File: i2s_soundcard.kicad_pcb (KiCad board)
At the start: 4 copper layers, 83.1 x 96.6 mm, 41 parts, among them J1 Conn_01x08, J2 Conn_01x06, J3 Conn_02x20_Odd_Even, J5 Conn_01x03, U1 TLV320AIC3206IRSBR, U2 TPA2006D1DRBR, U3 TPA2006D1DRBR, U4 FSA2275UMX, U6 TLV7111830DSER, U7 TPD4E02B04DQAR, U8 TPD4E02B04DQAR

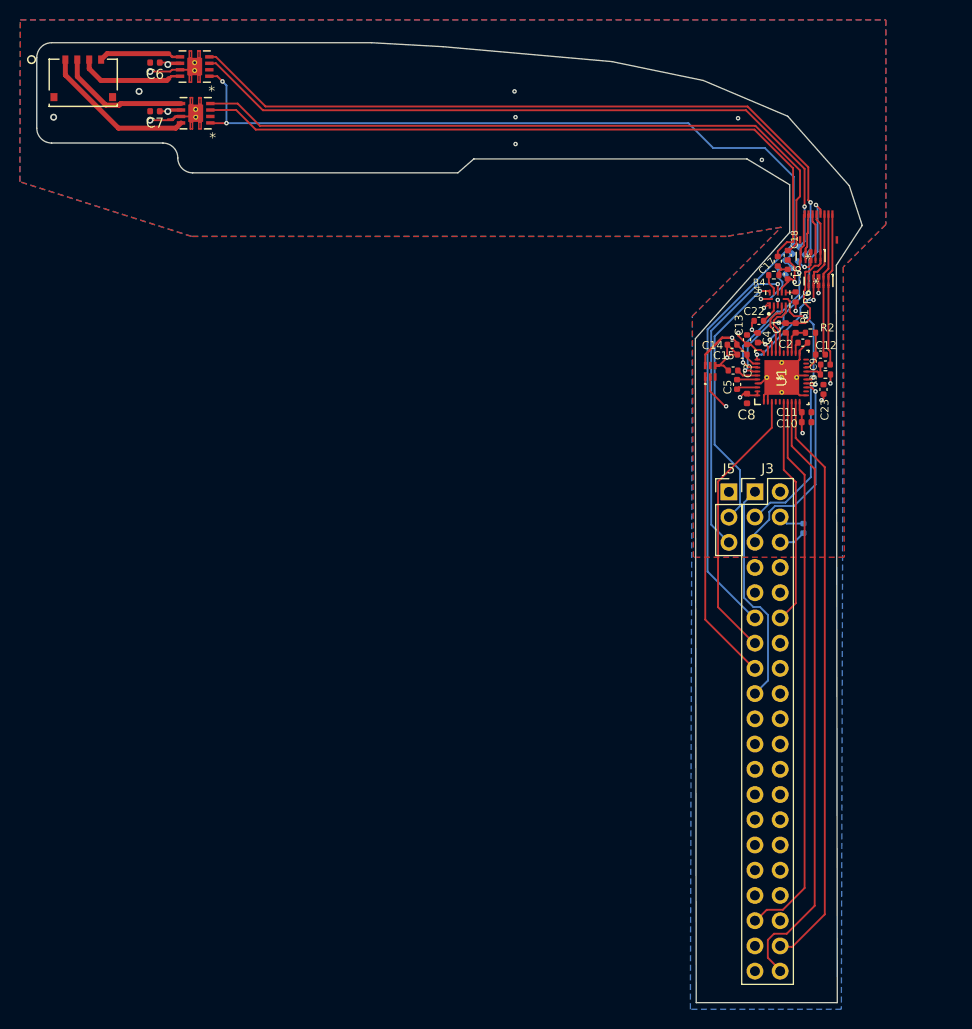
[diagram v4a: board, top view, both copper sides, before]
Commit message: Add 27R resistors to transmit side of i2s lines as recommended by aic3206 datasheet.
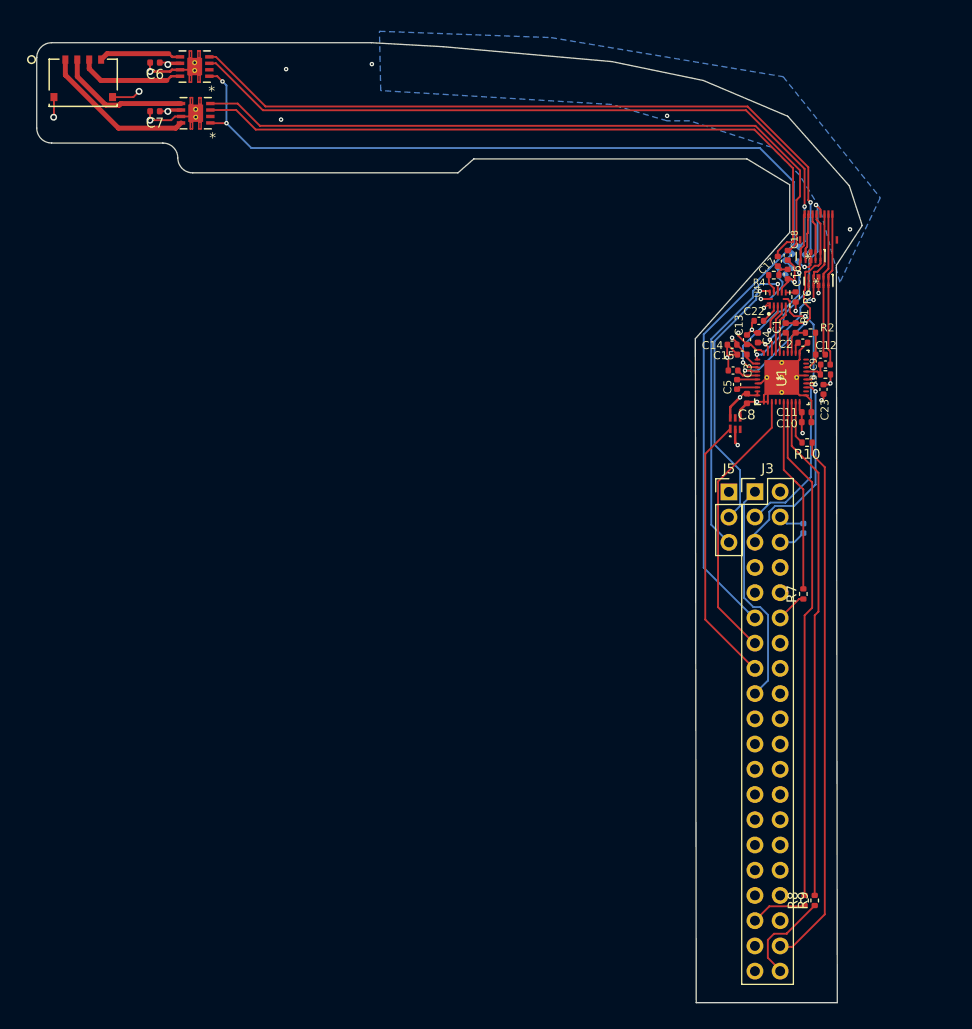
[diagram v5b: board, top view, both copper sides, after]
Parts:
- added R10: 27, Resistor_SMD:R_0402_1005Metric, F.Cu at (165.4, 98.6)
- added R7: 27, Resistor_SMD:R_0402_1005Metric, F.Cu at (165.0, 113.8)
- added R8: 27, Resistor_SMD:R_0402_1005Metric, F.Cu at (165.1, 144.7)
- added R9: 27, Resistor_SMD:R_0402_1005Metric, F.Cu at (166.1, 144.7)
- moved U6 5.84 mm to (158.1, 96.6)
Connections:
- U1 pad 6: /BCLK -> Net-(U1-Pad6)
- U1 pad 7: /WCLK -> Net-(U1-Pad7)
- U1 pad 8: /DIN -> Net-(U1-Pad8)
- U1 pad 9: /DOUT -> Net-(U1-Pad9)
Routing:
- net /DIN: track 61.7 -> 10.00 mm
- net Net-(U1-Pad7): track 0.00 -> 51.0 mm
- net Net-(U1-Pad8): track 0.00 -> 51.0 mm
- net /WCLK: track 56.1 -> 5.63 mm
- net /BCLK: track 23.0 -> 3.12 mm
- net Net-(U1-Pad6): track 0.00 -> 19.8 mm
- net GND: track 51.9 -> 67.6 mm, vias 17 -> 18
- net /DOUT: track 58.7 -> 53.9 mm
- net Net-(U1-Pad9): track 0.00 -> 4.37 mm
- net /LDO_EN1: track 31.6 -> 27.3 mm
- net /VCC1.8: track 12.6 -> 10.6 mm
- net /VSYS: track 15.7 -> 13.7 mm
- net /~AMP_SHUTDOWN: track 117.5 -> 116.7 mm
- net /CODEC_LOL: track 5.78 -> 5.09 mm
- net /CODEC_LOR: track 5.73 -> 5.05 mm
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- added copper zone on In2.Cu, net /IOVDD
- removed copper zone on F.Cu, net GND

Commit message: cleanup
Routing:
- net GND: vias 18 -> 15
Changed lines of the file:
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@@
   (net 62 "/MCLK")
   (net 63 "unconnected-(U1-Pad12)")
-  (net 64 "Net-(U1-Pad6)")
+  (net 64 "Net-(R7-Pad2)")
   (net 65 "unconnected-(U1-Pad19)")
   (net 66 "unconnected-(U1-Pad20)")
@@
   (net 77 "/CODEC_LOR")
   (net 78 "/SPKR_LO_SEL")
-  (net 79 "Net-(U1-Pad7)")
-  (net 80 "Net-(U1-Pad8)")
-  (net 81 "Net-(U1-Pad9)")
+  (net 79 "Net-(R8-Pad2)")
+  (net 80 "Net-(R9-Pad2)")
+  (net 81 "Net-(R10-Pad2)")
   (footprint "footprints:FF18-8A-R11AD-B-3H" (layer "F.Cu")
     (at 166.5 76.85 180)
@@
       (net 27 "/BCLK") (pintype "passive"))
     (pad "2" smd roundrect (at 0.51 0 90) (locked) (size 0.54 0.64) (layers "F.Cu" "F.Paste" "F.Mask") (roundrect_rratio 0.25)
-      (net 64 "Net-(U1-Pad6)") (pintype "passive"))
+      (net 64 "Net-(R7-Pad2)") (pintype "passive"))
     (model "${KICAD6_3DMODEL_DIR}/Resistor_SMD.3dshapes/R_0402_1005Metric.wrl"
       (offset (xyz 0 0 0))
@@
       (net 30 "/DOUT") (pintype "passive"))
     (pad "2" smd roundrect (at 0.51 0 180) (locked) (size 0.54 0.64) (layers "F.Cu" "F.Paste" "F.Mask") (roundrect_rratio 0.25)
-      (net 81 "Net-(U1-Pad9)") (pintype "passive"))
+      (net 81 "Net-(R10-Pad2)") (pintype "passive"))
     (model "${KICAD6_3DMODEL_DIR}/Resistor_SMD.3dshapes/R_0402_1005Metric.wrl"
       (offset (xyz 0 0 0))
@@
       (net 28 "/WCLK") (pintype "passive"))
     (pad "2" smd roundrect (at 0.51 0 90) (locked) (size 0.54 0.64) (layers "F.Cu" "F.Paste" "F.Mask") (roundrect_rratio 0.25)
-      (net 79 "Net-(U1-Pad7)") (pintype "passive"))
+      (net 79 "Net-(R8-Pad2)") (pintype "passive"))
     (model "${KICAD6_3DMODEL_DIR}/Resistor_SMD.3dshapes/R_0402_1005Metric.wrl"
       (offset (xyz 0 0 0))
@@
       (net 29 "/DIN") (pintype "passive"))
     (pad "2" smd roundrect (at 0.51 0 90) (locked) (size 0.54 0.64) (layers "F.Cu" "F.Paste" "F.Mask") (roundrect_rratio 0.25)
-      (net 80 "Net-(U1-Pad8)") (pintype "passive"))
+      (net 80 "Net-(R9-Pad2)") (pintype "passive"))
     (model "${KICAD6_3DMODEL_DIR}/Resistor_SMD.3dshapes/R_0402_1005Metric.wrl"
       (offset (xyz 0 0 0))
@@
       (net 62 "/MCLK") (pinfunction "MCLK") (pintype "input"))
     (pad "6" smd oval (at -2.45 0.2 180) (locked) (size 0.2 0.599999) (layers "F.Cu" "F.Paste" "F.Mask")
-      (net 64 "Net-(U1-Pad6)") (pinfunction "BCLK") (pintype "bidirectional"))
+      (net 64 "Net-(R7-Pad2)") (pinfunction "BCLK") (pintype "bidirectional"))
     (pad "7" smd oval (at -2.45 0.599999 180) (locked) (size 0.2 0.599999) (layers "F.Cu" "F.Paste" "F.Mask")
-      (net 79 "Net-(U1-Pad7)") (pinfunction "WCLK") (pintype "bidirectional"))
+      (net 79 "Net-(R8-Pad2)") (pinfunction "WCLK") (pintype "bidirectional"))
     (pad "8" smd oval (at -2.45 0.999998 180) (locked) (size 0.2 0.599999) (layers "F.Cu" "F.Paste" "F.Mask")
-      (net 80 "Net-(U1-Pad8)") (pinfunction "DIN_MFP1") (pintype "input"))
+      (net 80 "Net-(R9-Pad2)") (pinfunction "DIN_MFP1") (pintype "input"))
     (pad "9" smd oval (at -2.45 1.4 180) (locked) (size 0.2 0.599999) (layers "F.Cu" "F.Paste" "F.Mask")
-      (net 81 "Net-(U1-Pad9)") (pinfunction "DOUT_MFP2") (pintype "output"))
+      (net 81 "Net-(R10-Pad2)") (pinfunction "DOUT_MFP2") (pintype "output"))
     (pad "10" smd oval (at -2.45 1.799999 180) (locked) (size 0.2 0.599999) (layers "F.Cu" "F.Paste" "F.Mask")
       (net 24 "/IOVDD") (pinfunction "IOVDD") (pintype "power_in"))
@@
   (via (at 99.2 61.2) (size 0.7) (drill 0.4) (layers "F.Cu" "B.Cu") (net 2))
   (via (at 99.2 66.1) (size 0.7) (drill 0.4) (layers "F.Cu" "B.Cu") (net 2))
-  (via (at 112.395 66.04) (size 0.45) (drill 0.2) (layers "F.Cu" "B.Cu") (free) (net 2))
   (via (at 98.1 63.2) (size 0.7) (drill 0.4) (layers "F.Cu" "B.Cu") (net 2))
   (via (at 160.312 94.45) (size 0.45) (drill 0.2) (layers "F.Cu" "B.Cu") (net 2))
   (via (at 159.8 87.2) (size 0.45) (drill 0.2) (layers "F.Cu" "B.Cu") (net 2))
   (via (at 167.7 92.6) (size 0.45) (drill 0.2) (layers "F.Cu" "B.Cu") (net 2))
-  (via (at 121.539 60.452) (size 0.45) (drill 0.2) (layers "F.Cu" "B.Cu") (free) (net 2))
   (via (at 166.5 83.5) (size 0.45) (drill 0.2) (layers "F.Cu" "B.Cu") (net 2))
   (via (at 161.544 87.249) (size 0.45) (drill 0.2) (layers "F.Cu" "B.Cu") (net 2))
@@
   (via (at 169.672 77.089) (size 0.45) (drill 0.2) (layers "F.Cu" "B.Cu") (free) (net 2))
   (via (at 165.1 80.875017) (size 0.45) (drill 0.2) (layers "F.Cu" "B.Cu") (net 2))
-  (via (at 112.903 60.96) (size 0.45) (drill 0.2) (layers "F.Cu" "B.Cu") (free) (net 2))
   (via (at 89.5 65.8) (size 0.7) (drill 0.4) (layers "F.Cu" "B.Cu") (net 2))
   (via (at 157.3 90) (size 0.45) (drill 0.2) (layers "F.Cu" "B.Cu") (net 2))

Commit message: Refactor everything but headers into a hierarchical sheet.
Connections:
- net /CODEC_LOL renamed /codec and amp/CODEC_LOL
- net /CODEC_LOR renamed /codec and amp/CODEC_LOR
- net /DETECT? renamed /codec and amp/DETECT?
- net /INTMIC_N renamed /codec and amp/INTMIC_N
- net /INTMIC_P renamed /codec and amp/INTMIC_P
- net /MCLK renamed /codec and amp/MCLK
- net /RING1 renamed /codec and amp/RING1
- net /RING2 renamed /codec and amp/RING2
- net /RING2_AGAIN renamed /codec and amp/RING2_AGAIN
- net /SLEEVE renamed /codec and amp/SLEEVE
- net /SPKR_L renamed /codec and amp/SPKR_L
- net /SPKR_LO_SEL renamed /codec and amp/SPKR_LO_SEL
- net /SPKR_R renamed /codec and amp/SPKR_R
- net /TIP renamed /codec and amp/TIP
- net /VCC1.8 renamed /codec and amp/VCC1.8
- net /spkr_amp_left/SPKR+ renamed /codec and amp/spkr_amp_left/SPKR+
- net /spkr_amp_left/SPKR- renamed /codec and amp/spkr_amp_left/SPKR-
- net /spkr_amp_right/SPKR+ renamed /codec and amp/spkr_amp_right/SPKR+
- net /spkr_amp_right/SPKR- renamed /codec and amp/spkr_amp_right/SPKR-
